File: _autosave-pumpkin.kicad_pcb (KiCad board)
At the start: 4 copper layers, 51 x 45.1 mm, 24 parts, among them J1 MK-12C02

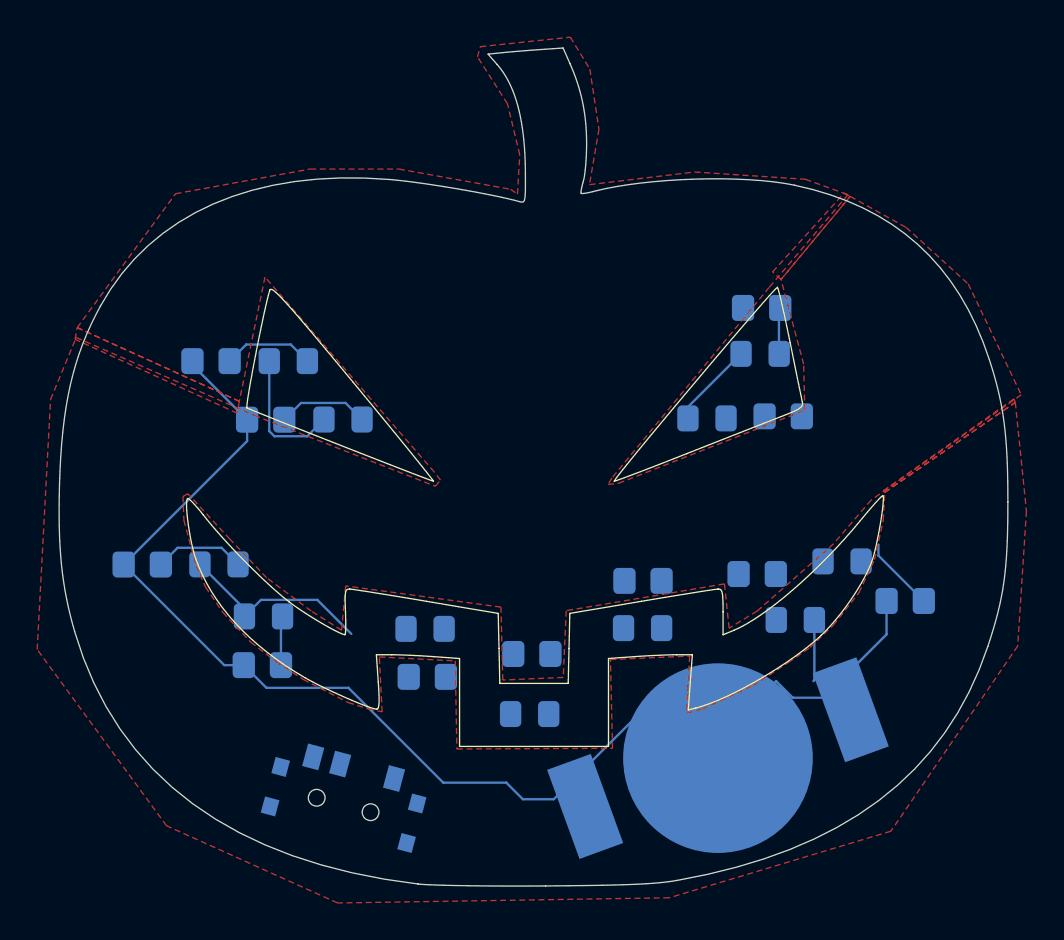
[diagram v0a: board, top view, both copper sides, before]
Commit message: changed cr2032 to cr1225
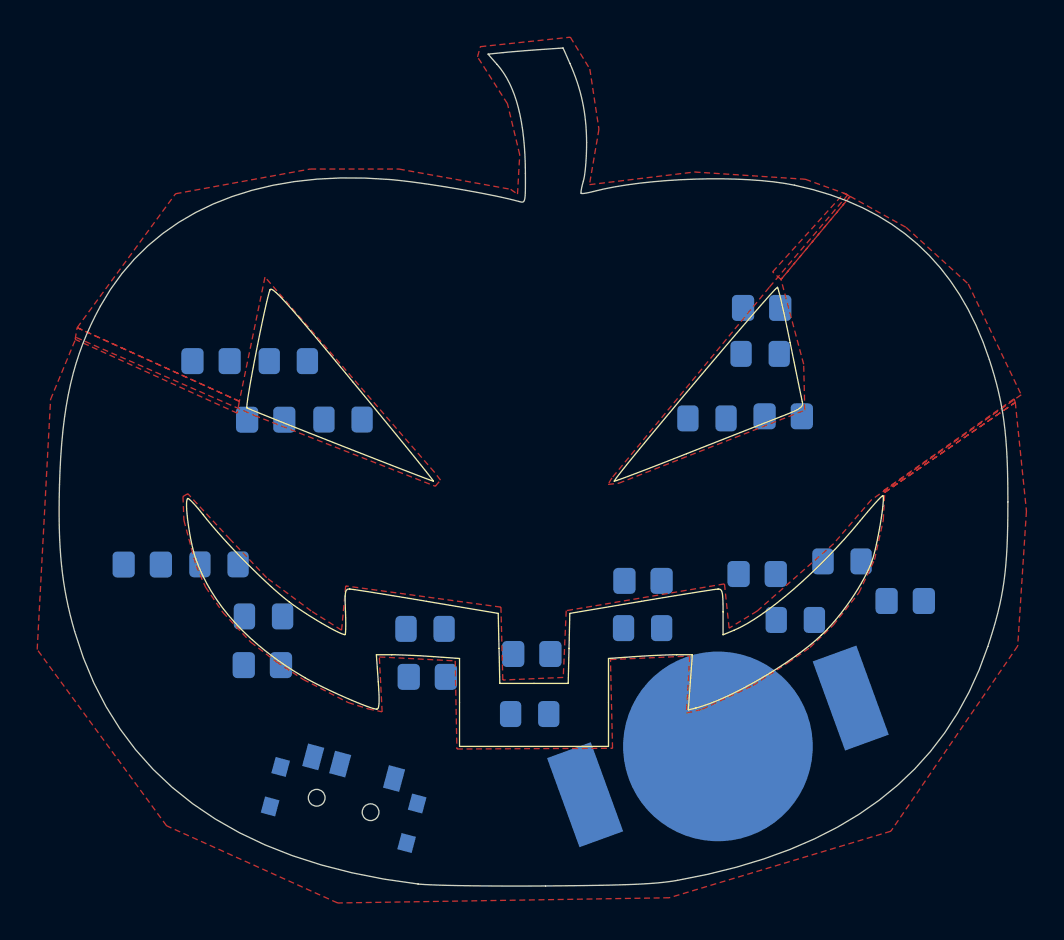
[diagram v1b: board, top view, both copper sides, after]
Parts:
- moved BT1 0.63 mm to (155.0, 110.1)
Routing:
- net GND: track 68.1 -> 0.00 mm
- net Net-(D1-A): track 22.5 -> 0.00 mm
- net Net-(D3-K): track 4.92 -> 0.00 mm
- net Net-(D1-K): track 4.92 -> 0.00 mm
- net Net-(D5-K): track 4.89 -> 0.00 mm
- net Net-(D11-K): track 4.04 -> 0.00 mm
- net Net-(D10-K): track 3.31 -> 0.00 mm
- net Net-(D6-K): track 2.66 -> 0.00 mm
- net Net-(D2-K): track 2.50 -> 0.00 mm
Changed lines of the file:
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@@
   )
   (footprint "Battery:BatteryHolder_LINX_BAT-HLD-012-SMT" (layer "B.Cu")
-    (at 155.03 110.76 -160)
+    (at 155.028336 110.129353 -160)
     (descr "SMT battery holder for CR1216/1220/1225, https://linxtechnologies.com/wp/wp-content/uploads/bat-hld-012-smt.pdf")
     (tags "battery holder coin cell cr1216 cr1220 cr1225")
@@
   (gr_curve (pts (xy 120.433712 103.948018) (xy 119.735219 101.537666) (xy 119.525189 99.501658) (xy 119.62 96.06))
     (stroke (width 0.054) (type solid)) (layer "Edge.Cuts"))
-  (segment (start 164.1 102.31) (end 164.1 104.102961) (width 0.127) (layer "B.Cu") (net 2))
-  (segment (start 157.1295 107.6505) (end 153.3005 107.6505) (width 0.127) (layer "B.Cu") (net 2))
-  (segment (start 158.16 106.62) (end 157.1295 107.6505) (width 0.127) (layer "B.Cu") (net 2))
-  (segment (start 129.71 92.56) (end 129.71 93.71) (width 0.127) (layer "B.Cu") (net 2))
-  (segment (start 144.5405 112.9705) (end 146.1995 112.9705) (width 0.127) (layer "B.Cu") (net 2))
-  (segment (start 143.65 112.08) (end 144.5405 112.9705) (width 0.127) (layer "B.Cu") (net 2))
-  (segment (start 123.07 100.35) (end 128.48 105.76) (width 0.127) (layer "B.Cu") (net 2))
-  (segment (start 128.48 105.76) (end 129.53 105.76) (width 0.127) (layer "B.Cu") (net 2))
-  (segment (start 153.3005 107.6505) (end 152.41 106.76) (width 0.127) (layer "B.Cu") (net 2))
-  (segment (start 160.692461 107.5105) (end 159.0505 107.5105) (width 0.127) (layer "B.Cu") (net 2))
-  (segment (start 129.71 93.71) (end 123.07 100.35) (width 0.127) (layer "B.Cu") (net 2))
-  (segment (start 135.16 106.98) (end 140.26 112.08) (width 0.127) (layer "B.Cu") (net 2))
-  (segment (start 146.1995 112.9705) (end 152.41 106.76) (width 0.127) (layer "B.Cu") (net 2))
-  (segment (start 126.77 89.41) (end 126.77 89.62) (width 0.127) (layer "B.Cu") (net 2))
-  (segment (start 129.53 105.76) (end 130.75 106.98) (width 0.127) (layer "B.Cu") (net 2))
-  (segment (start 140.26 112.08) (end 143.65 112.08) (width 0.127) (layer "B.Cu") (net 2))
-  (segment (start 130.75 106.98) (end 135.16 106.98) (width 0.127) (layer "B.Cu") (net 2))
-  (segment (start 164.1 104.102961) (end 160.692461 107.5105) (width 0.127) (layer "B.Cu") (net 2))
-  (segment (start 159.0505 107.5105) (end 158.16 106.62) (width 0.127) (layer "B.Cu") (net 2))
-  (segment (start 126.77 89.62) (end 129.71 92.56) (width 0.127) (layer "B.Cu") (net 2))
-  (segment (start 132.0595 88.5195) (end 132.95 89.41) (width 0.127) (layer "B.Cu") (net 3))
-  (segment (start 129.6605 88.5195) (end 132.0595 88.5195) (width 0.127) (layer "B.Cu") (net 3))
-  (segment (start 128.77 89.41) (end 129.6605 88.5195) (width 0.127) (layer "B.Cu") (net 3))
-  (segment (start 130.4555 102.2495) (end 133.4845 102.2495) (width 0.127) (layer "B.Cu") (net 4))
-  (segment (start 130.9 89.41) (end 130.9 93.172961) (width 0.127) (layer "B.Cu") (net 4))
-  (segment (start 130.9 93.172961) (end 131.177539 93.4505) (width 0.127) (layer "B.Cu") (net 4))
-  (segment (start 133.4845 102.2495) (end 135.315 104.08) (width 0.127) (layer "B.Cu") (net 4))
-  (segment (start 132.942 93.4505) (end 133.8425 92.55) (width 0.127) (layer "B.Cu") (net 4))
-  (segment (start 129.565 102.7325) (end 129.565 103.14) (width 0.127) (layer "B.Cu") (net 4))
-  (segment (start 127.1725 100.34) (end 129.565 102.7325) (width 0.127) (layer "B.Cu") (net 4))
-  (segment (start 153.415 92.49) (end 153.415 91.8775) (width 0.127) (layer "B.Cu") (net 4))
-  (segment (start 153.415 91.8775) (end 156.2725 89.02) (width 0.127) (layer "B.Cu") (net 4))
-  (segment (start 131.177539 93.4505) (end 132.942 93.4505) (width 0.127) (layer "B.Cu") (net 4))
-  (segment (start 129.565 103.14) (end 130.4555 102.2495) (width 0.127) (layer "B.Cu") (net 4))
-  (segment (start 158.31 89.0075) (end 158.3225 89.02) (width 0.127) (layer "B.Cu") (net 5))
-  (segment (start 158.31 86.53) (end 158.31 89.0075) (width 0.127) (layer "B.Cu") (net 5))
-  (segment (start 131.71 92.56) (end 132.6105 91.6595) (width 0.127) (layer "B.Cu") (net 6))
-  (segment (start 132.6105 91.6595) (end 135.002 91.6595) (width 0.127) (layer "B.Cu") (net 6))
-  (segment (start 135.002 91.6595) (end 135.8925 92.55) (width 0.127) (layer "B.Cu") (net 6))
-  (segment (start 125.9705 99.4495) (end 128.332 99.4495) (width 0.127) (layer "B.Cu") (net 8))
-  (segment (start 125.07 100.35) (end 125.9705 99.4495) (width 0.127) (layer "B.Cu") (net 8))
-  (segment (start 128.332 99.4495) (end 129.2225 100.34) (width 0.127) (layer "B.Cu") (net 8))
-  (segment (start 131.53 103.225) (end 131.615 103.14) (width 0.127) (layer "B.Cu") (net 9))
-  (segment (start 131.53 105.76) (end 131.53 103.225) (width 0.127) (layer "B.Cu") (net 9))
-  (segment (start 160.215 103.33) (end 160.215 106.565) (width 0.127) (layer "B.Cu") (net 13))
-  (segment (start 160.215 106.565) (end 160.16 106.62) (width 0.127) (layer "B.Cu") (net 13))
-  (segment (start 163.6625 99.28) (end 163.6625 99.8725) (width 0.127) (layer "B.Cu") (net 14))
-  (segment (start 163.6625 99.8725) (end 166.1 102.31) (width 0.127) (layer "B.Cu") (net 14))
   (zone (net 2) (net_name "GND") (layer "F.Cu") (hatch edge 0.5)
     (connect_pads (clearance 0.5))
